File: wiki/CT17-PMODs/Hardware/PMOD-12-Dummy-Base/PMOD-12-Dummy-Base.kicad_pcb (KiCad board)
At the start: 2 copper layers, 40.2 x 23.3 mm, 1 part, among them J1 Conn_02x06_Top_Bottom_Mountin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

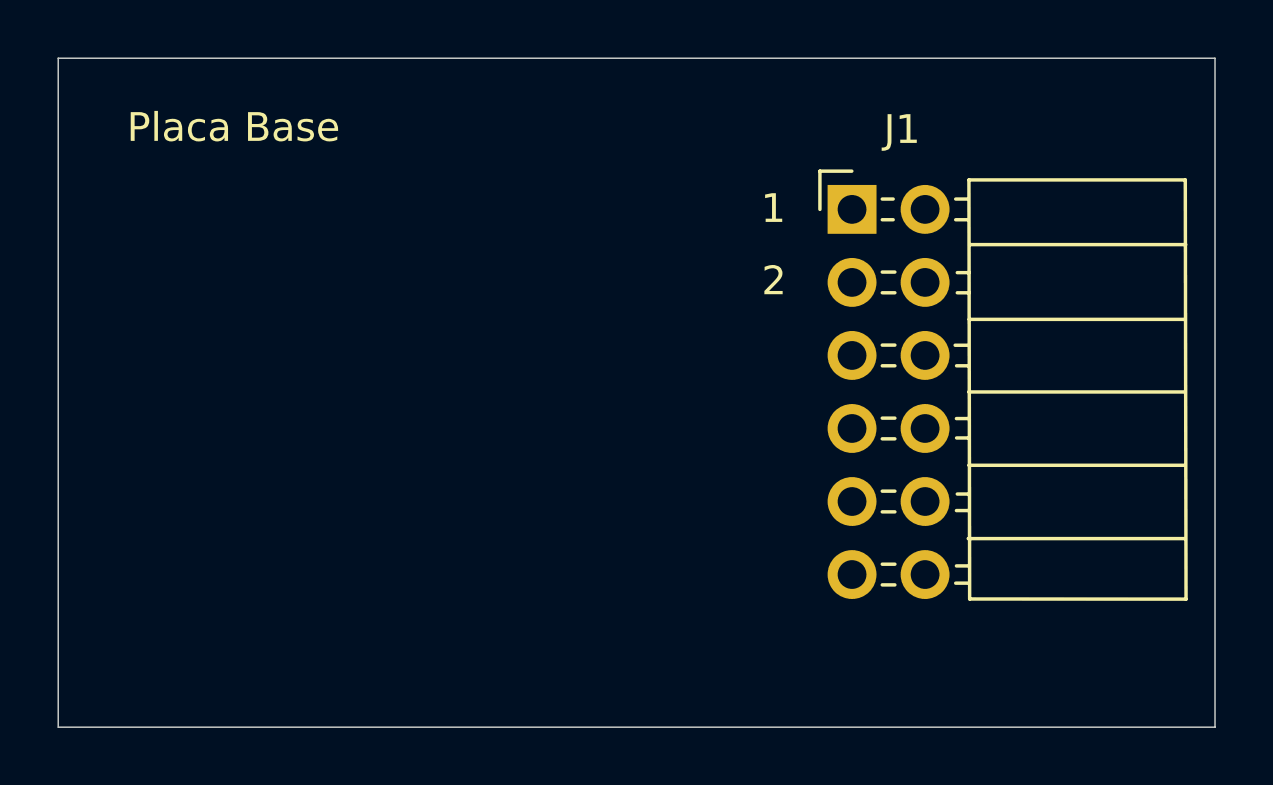
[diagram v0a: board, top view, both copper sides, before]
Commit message: CT17: Add PMOD-12-Dummy-Base kicad files
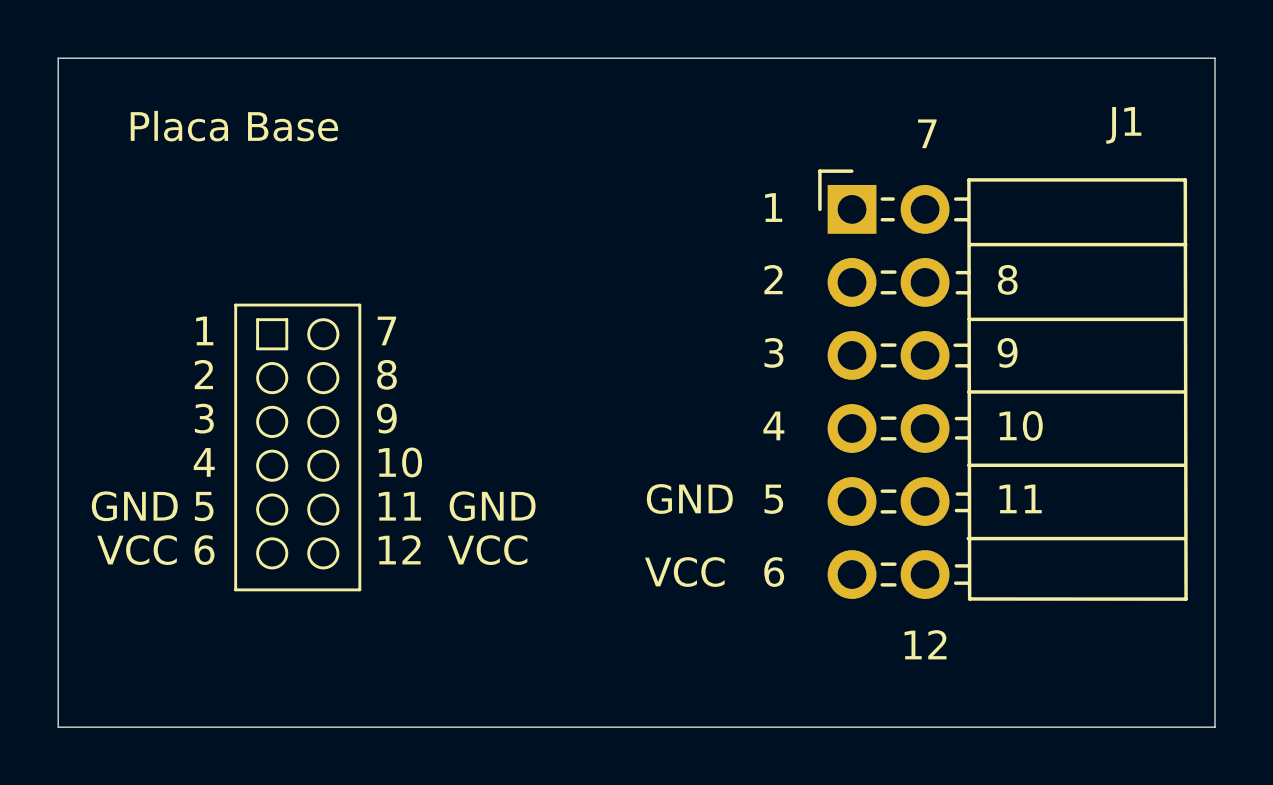
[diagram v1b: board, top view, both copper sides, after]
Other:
- board text added: "10"
- board text added: "11"
- board text added: "12"
- board text added: "3"
- board text added: "4"
- board text added: "5"
- board text added: "6"
- board text added: "7"
- board text added: "8"
- board text added: "9"
- board text added: "GND"
- board text added: "VCC"
